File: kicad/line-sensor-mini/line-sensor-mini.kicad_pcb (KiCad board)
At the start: 2 copper layers, 28.7 x 81.3 mm, 25 parts, among them J1 SENSORS, Q1 BC337, Q2 Q_Photo_NPN, Q3 Q_Photo_NPN, Q4 Q_Photo_NPN, Q5 Q_Photo_NPN

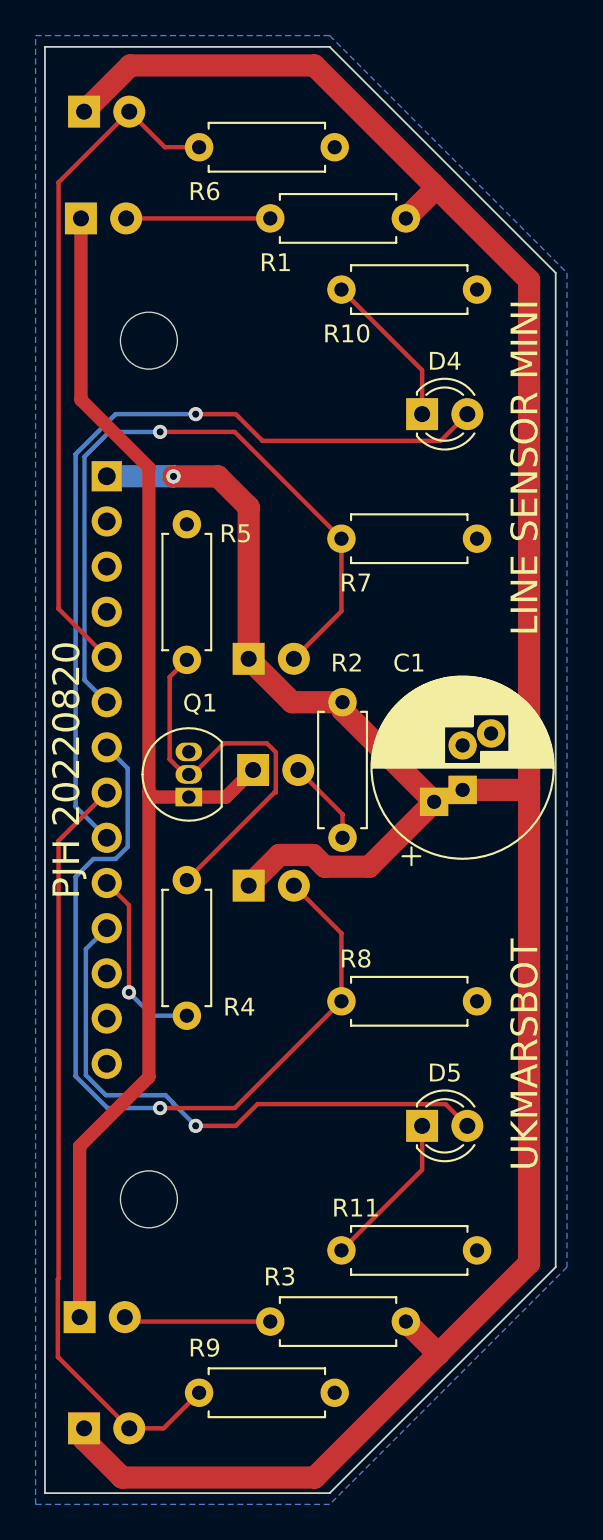
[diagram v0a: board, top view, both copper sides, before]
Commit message: rename to line-sensor-mini
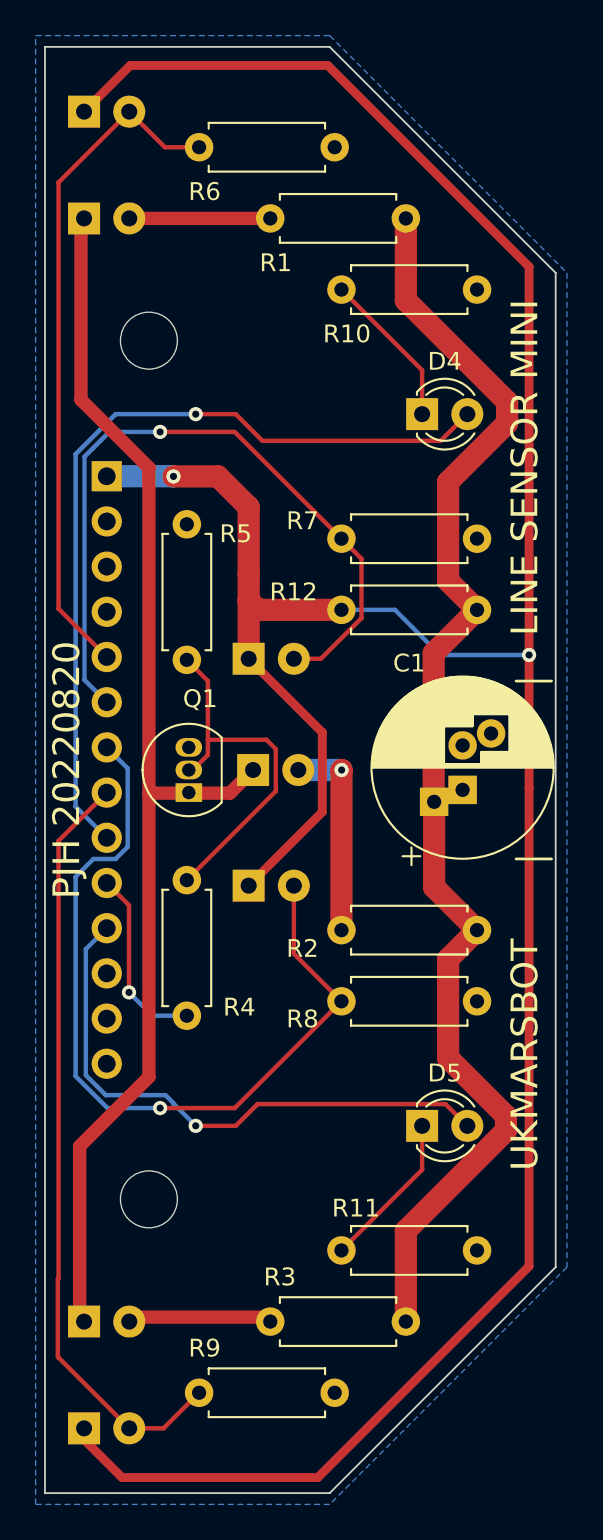
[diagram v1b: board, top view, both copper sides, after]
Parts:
- added R12: 33R, Resistor_THT:R_Axial_DIN0207_L6.3mm_D2.5mm_P7.62mm_Horizontal, F.Cu at (162.8, 96.0)
- moved R2 14.9 mm to (162.8, 114.0), turned to 180 degrees
- moved D3 0.35 mm to (140.7, 136.0)
- moved Q1 0.25 mm to (146.6, 106.3)
- moved D1 0.17 mm to (140.7, 74.0)
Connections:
- C1 pad 1: 5V -> /5V_EMITTERS
- R1 pad 2: 5V -> /5V_EMITTERS
- R2 pad 1: 5V -> /5V_EMITTERS
- R3 pad 2: 5V -> /5V_EMITTERS
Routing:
- net /5V_EMITTERS: track 0.00 -> 72.8 mm
- net Net-(D2-Pad2): track 4.84 -> 11.4 mm, vias 0 -> 1
- net 5V: track 170.9 -> 168.8 mm, vias 1 -> 2
- net A2_LEFT_LINE: track 39.7 -> 41.5 mm
- net Net-(Q1-Pad2): track 22.5 -> 20.7 mm
